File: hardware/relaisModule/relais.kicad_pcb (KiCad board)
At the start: 2 copper layers, 188 x 97 mm, 104 parts, among them J1 Button-Sensors-MicroMatch2X03, J10 WAGO2604-1104, J11 WAGO2604-1104, J12 RJ45-CAN, J13 WAGO2604-1102, J2 WAGO2604-1104, J4 WAGO2604-1104, J5 IRDA, J6 IRDA, J7 RJ45-CAN, J8 WAGO2604-1104, J9 WAGO2604-1104, K1 RT314A12, K10 RT314A12, K11 RT314A12, K12 RT314A12, K2 RT314A12, K3 RT314A12, K4 RT314A12, K5 RT314A12, K6 RT314A12, K7 RT314A12, K8 RT314A12, K9 RT314A12, Q1 BC847, Q2 BC847, U1 PESD2CAN, U2 MCP2562-E-SN, U3 ESP32-WROOM-32, U4 MCP1703A-3302_SOT89, U5 PCF8574A, U6 PCF8574A, U7 TPL7407LADR, U8 TPL7407LADR, U9 wuerthDebug6

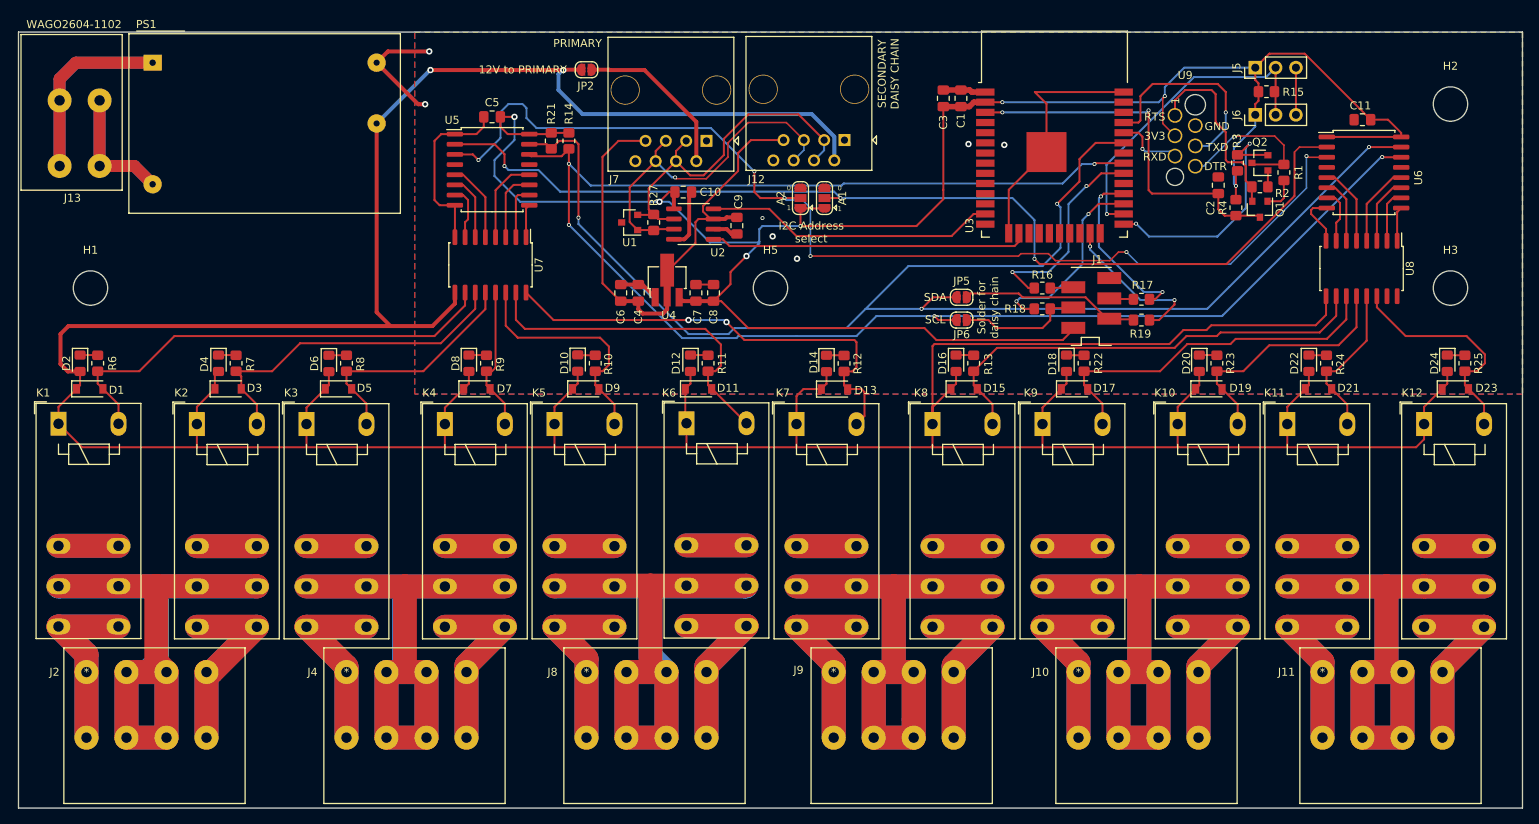
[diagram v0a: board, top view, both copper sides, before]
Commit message: feat: change PCB debug to EN/BOOT0
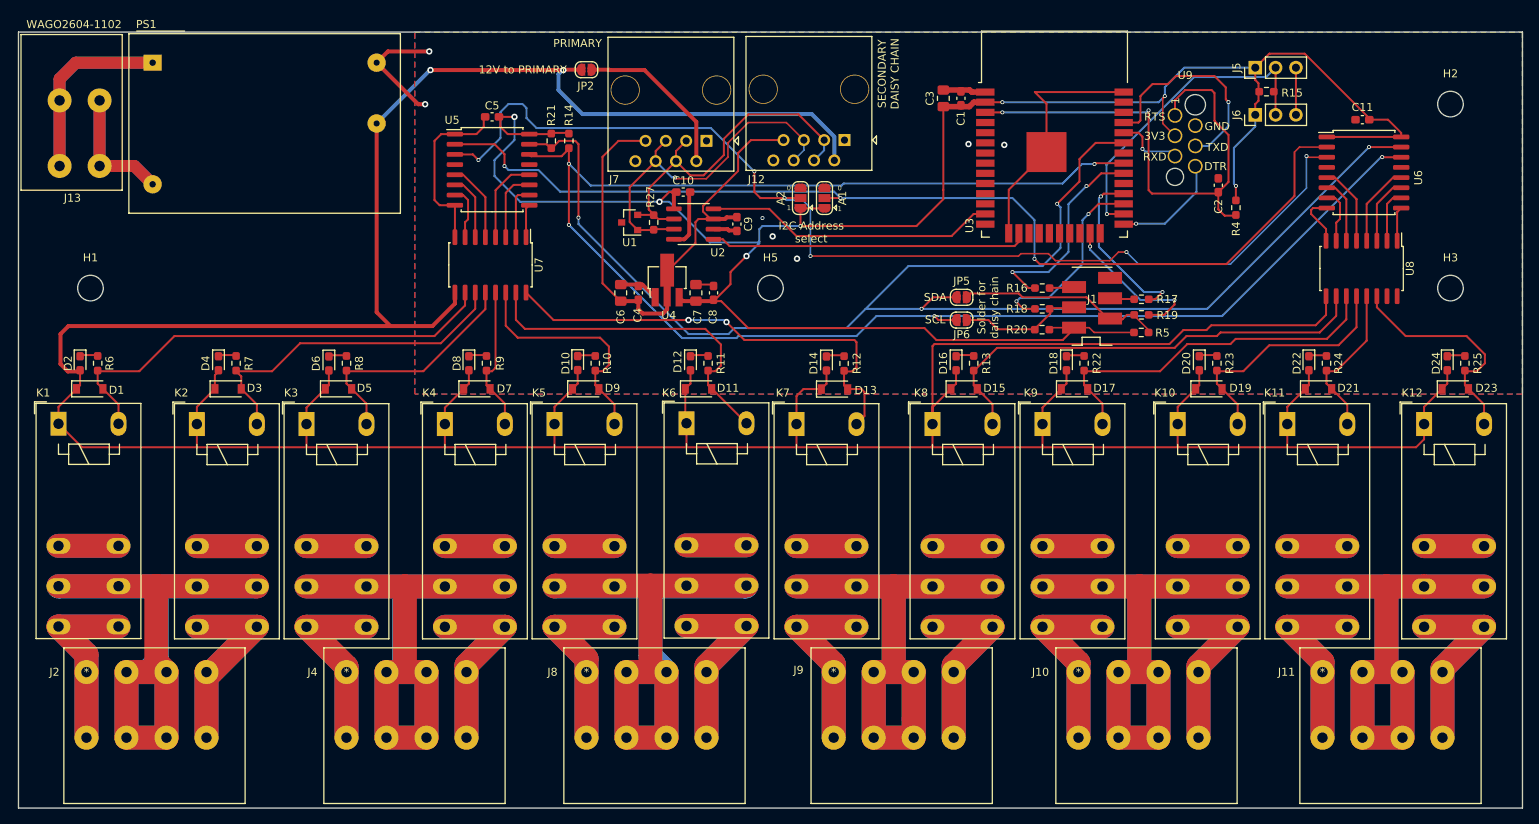
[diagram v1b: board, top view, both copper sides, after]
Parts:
- removed Q1, Q2: BC847, Package_TO_SOT_SMD:SOT-23
- removed R1, R2, R3: 10K, Resistor_SMD:R_0805_2012Metric_Pad1.20x1.40mm_HandSolder
- added R20: 2K2, Resistor_SMD:R_0603_1608Metric_Pad0.98x0.95mm_HandSolder, F.Cu at (161.9, 93.2)
- added R5: 2K2, Resistor_SMD:R_0603_1608Metric_Pad0.98x0.95mm_HandSolder, F.Cu at (174.3, 93.5)
- C1, C10, C11, C2, C4, C5, C8, C9: footprint Capacitor_SMD:C_0805_2012Metric_Pad1.18x1.45mm_HandSolder -> Capacitor_SMD:C_0603_1608Metric_Pad1.08x0.95mm_HandSolder
- D10, D12, D14, D16, D18, D2, D20, D22, D24, D4, D6, D8: footprint LED_SMD:LED_0805_2012Metric_Pad1.15x1.40mm_HandSolder -> LED_SMD:LED_0603_1608Metric_Pad1.05x0.95mm_HandSolder
- H1, H2, H3, H5: footprint MountingHole:MountingHole_4.3mm_M4_DIN965 -> MountingHole:MountingHole_3.2mm_M3_DIN965
- R10, R11, R12, R13, R14, R15, R16, R17, R18, R19, R21, R22, R23, R24, R25, R27, R4, R6, R7, R8, R9: footprint Resistor_SMD:R_0805_2012Metric_Pad1.20x1.40mm_HandSolder -> Resistor_SMD:R_0603_1608Metric_Pad0.98x0.95mm_HandSolder
- U5, U6: value PCF8574A -> PCA9534
- moved J1 5.99 mm to (168.2, 89.9), turned to 180 degrees
- moved R19 0.65 mm to (174.4, 91.3)
- moved C9 0.20 mm to (123.8, 80.0)
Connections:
- J1 pad 1: GND -> +3V3
- J1 pad 2: Net-(R16-Pad2) -> /SDA_EXT
- J1 pad 3: Net-(R17-Pad2) -> /SCL_EXT
- J1 pad 4: /SCL_EXT -> Net-(J1-Pad4)
- J1 pad 5: /SDA_EXT -> Net-(J1-Pad5)
- J1 pad 6: +3V3 -> GND
- R16 pad 2: Net-(R16-Pad2) -> Net-(J1-Pad5)
- R17 pad 2: Net-(R17-Pad2) -> Net-(J1-Pad4)
- U9 pad 1: /RTS -> /EN
- U9 pad 6: /DTR -> /BOOT0
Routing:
- net /RTS: track 24.0 -> 0.00 mm
- net /DTR: track 19.6 -> 0.00 mm, vias 1 -> 0
- net /EN: track 46.8 -> 64.9 mm
- net /BOOT0: track 31.8 -> 14.2 mm, vias 2 -> 1
- net +3V3: track 266.7 -> 275.4 mm
- net Net-(Q1-Pad1): track 4.42 -> 0.00 mm
- net /SDA_EXT: track 22.4 -> 25.6 mm
- net Net-(R16-Pad2): track 3.01 -> 0.00 mm
- net Net-(J1-Pad5): track 0.00 -> 3.01 mm
- net Net-(R17-Pad2): track 2.91 -> 0.00 mm
- net Net-(J1-Pad4): track 0.00 -> 2.91 mm
- net Net-(Q2-Pad1): track 2.05 -> 0.00 mm
- net /TXD: track 26.4 -> 27.8 mm

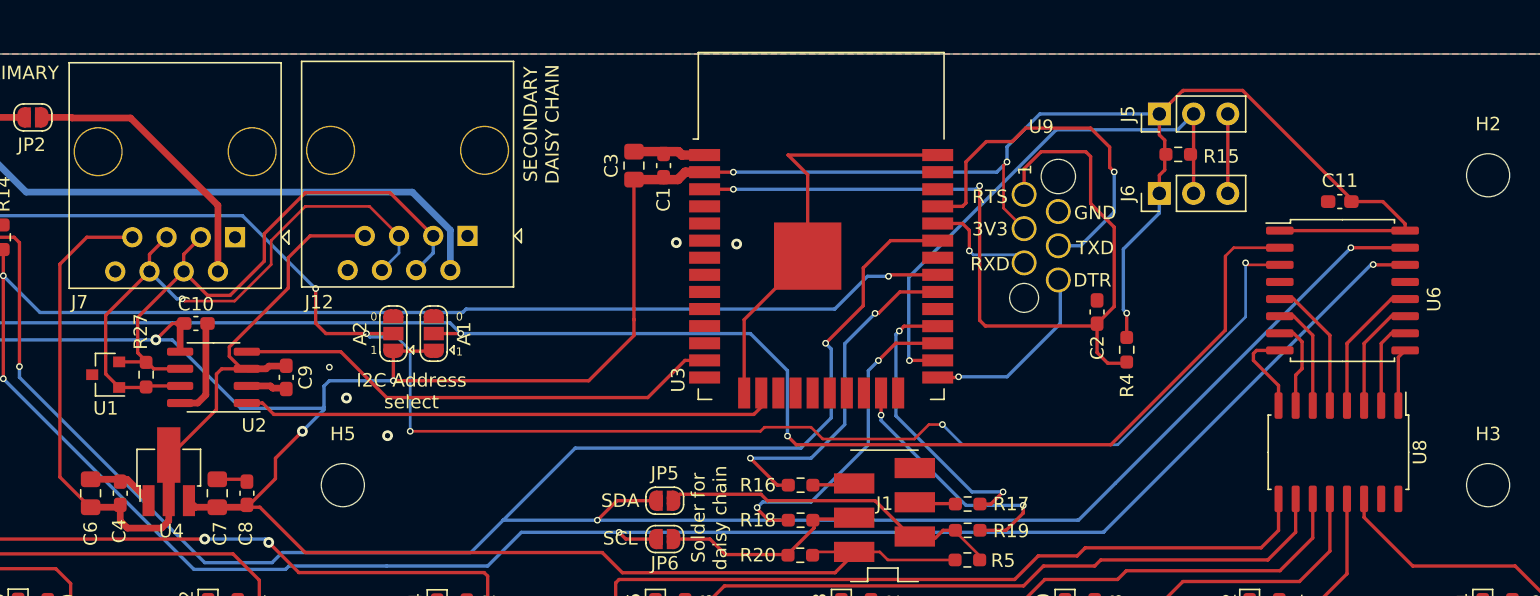
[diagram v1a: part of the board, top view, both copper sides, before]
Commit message: feat: Add fab export options for all pcbs
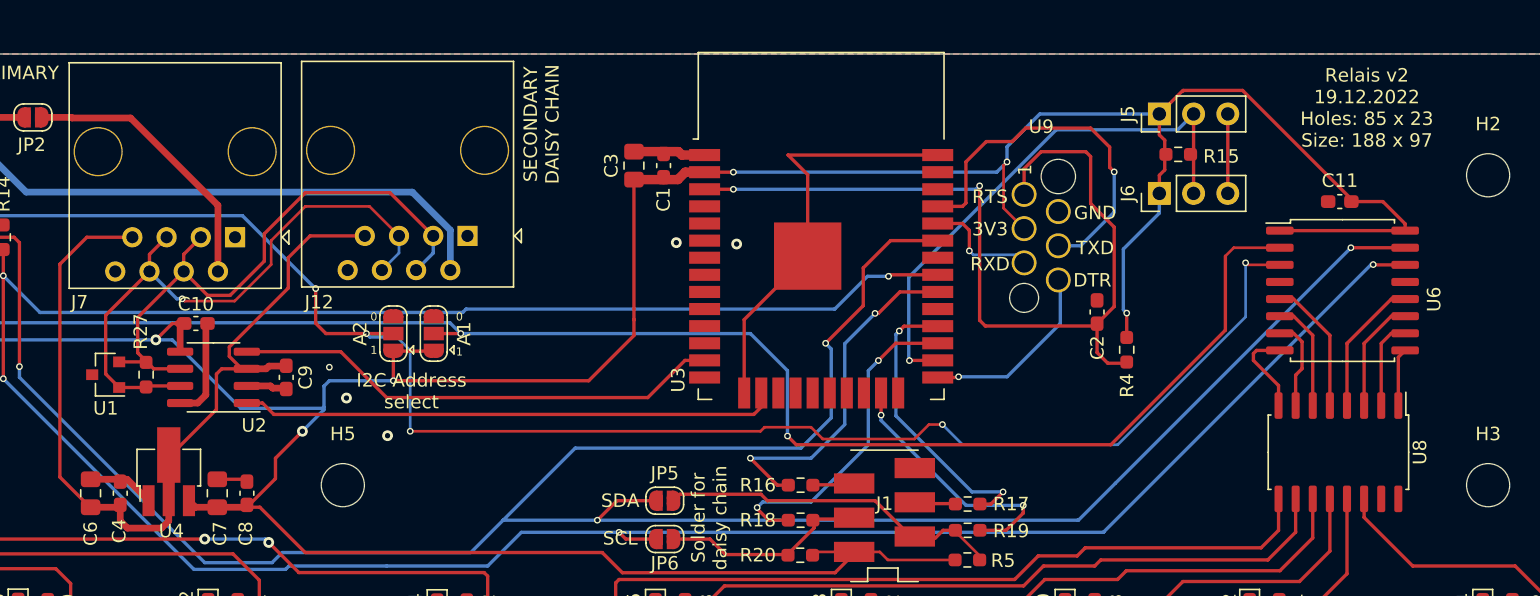
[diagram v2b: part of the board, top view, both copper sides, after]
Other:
- board text added: "Relais v2 19.12.2022 Holes: 85 x 23 Size: 188 x 97"
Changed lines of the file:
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@@
       (layerselection 0x00010fc_ffffffff)
       (disableapertmacros false)
-      (usegerberextensions true)
-      (usegerberattributes false)
+      (usegerberextensions false)
+      (usegerberattributes true)
       (usegerberadvancedattributes true)
       (creategerberjobfile true)
@@
       (plotinvisibletext false)
       (sketchpadsonfab false)
-      (subtractmaskfromsilk false)
+      (subtractmaskfromsilk true)
       (outputformat 1)
       (mirror false)
       (drillshape 0)
       (scaleselection 1)
-      (outputdirectory "fab")
+      (outputdirectory "relais-fab")
     )
   )
@@
     (fp_line (start -1 -0.625) (end 1 -0.625) (layer "F.Fab") (width 0.1))
     (fp_line (start 1 0.625) (end -1 0.625) (layer "F.Fab") (width 0.1))
-    (pad "1" smd roundrect (at -1.0375 0 90) (size 1.175 1.45) (layers "F.Cu" "F.Paste" "F.Mask") (roundrect_rratio 0.212766)
+    (pad "1" smd roundrect (at -1.0375 0 90) (size 1.175 1.45) (layers "F.Cu" "F.Paste" "F.Mask") (roundrect_rratio 0.2127659574)
       (net 5 "+3V3") (pintype "passive"))
-    (pad "2" smd roundrect (at 1.0375 0 90) (size 1.175 1.45) (layers "F.Cu" "F.Paste" "F.Mask") (roundrect_rratio 0.212766)
+    (pad "2" smd roundrect (at 1.0375 0 90) (size 1.175 1.45) (layers "F.Cu" "F.Paste" "F.Mask") (roundrect_rratio 0.2127659574)
       (net 4 "GND") (pintype "passive"))
     (model "${KICAD6_3DMODEL_DIR}/Capacitor_SMD.3dshapes/C_0805_2012Metric.wrl"
@@
     (fp_line (start -1 0.625) (end -1 -0.625) (layer "F.Fab") (width 0.1))
     (fp_line (start 1 -0.625) (end 1 0.625) (layer "F.Fab") (width 0.1))
-    (pad "1" smd roundrect locked (at -1.0375 0 90) (size 1.175 1.45) (layers "F.Cu" "F.Paste" "F.Mask") (roundrect_rratio 0.212766)
+    (pad "1" smd roundrect locked (at -1.0375 0 90) (size 1.175 1.45) (layers "F.Cu" "F.Paste" "F.Mask") (roundrect_rratio 0.2127659574)
       (net 6 "+5V") (pintype "passive"))
-    (pad "2" smd roundrect locked (at 1.0375 0 90) (size 1.175 1.45) (layers "F.Cu" "F.Paste" "F.Mask") (roundrect_rratio 0.212766)
+    (pad "2" smd roundrect locked (at 1.0375 0 90) (size 1.175 1.45) (layers "F.Cu" "F.Paste" "F.Mask") (roundrect_rratio 0.2127659574)
       (net 4 "GND") (pintype "passive"))
     (model "${KISYS3DMOD}/Capacitor_SMD.3dshapes/C_0805_2012Metric.wrl"
@@
     (fp_line (start -1 0.625) (end -1 -0.625) (layer "F.Fab") (width 0.1))
     (fp_line (start 1 -0.625) (end 1 0.625) (layer "F.Fab") (width 0.1))
-    (pad "1" smd roundrect locked (at -1.0375 0 90) (size 1.175 1.45) (layers "F.Cu" "F.Paste" "F.Mask") (roundrect_rratio 0.212766)
+    (pad "1" smd roundrect locked (at -1.0375 0 90) (size 1.175 1.45) (layers "F.Cu" "F.Paste" "F.Mask") (roundrect_rratio 0.2127659574)
       (net 5 "+3V3") (pintype "passive"))
-    (pad "2" smd roundrect locked (at 1.0375 0 90) (size 1.175 1.45) (layers "F.Cu" "F.Paste" "F.Mask") (roundrect_rratio 0.212766)
+    (pad "2" smd roundrect locked (at 1.0375 0 90) (size 1.175 1.45) (layers "F.Cu" "F.Paste" "F.Mask") (roundrect_rratio 0.2127659574)
       (net 4 "GND") (pintype "passive"))
     (model "${KISYS3DMOD}/Capacitor_SMD.3dshapes/C_0805_2012Metric.wrl"
@@
     (effects (font (size 0.6 0.6) (thickness 0.08)))
   )
+  (gr_text "Relais v2\n19.12.2022\nHoles: 85 x 23\nSize: 188 x 97" (at 204 60) (layer "F.SilkS")
+    (effects (font (size 1 1) (thickness 0.15)))
+  )
   (segment (start 197.5405 70.379) (end 194.121 70.379) (width 0.2) (layer "F.Cu") (net 2))
